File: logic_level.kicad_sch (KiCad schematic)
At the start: 0 parts

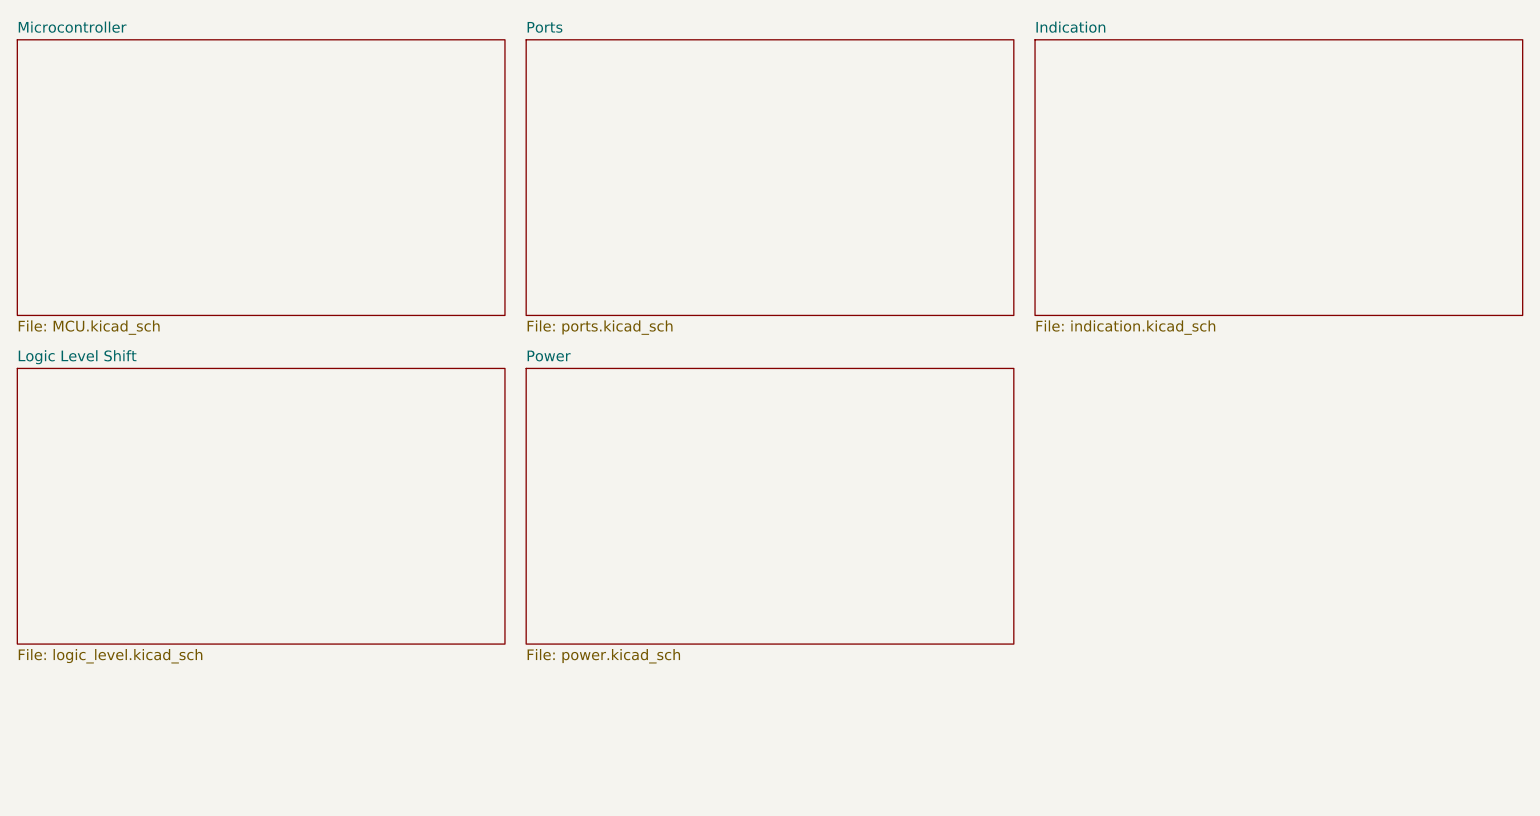
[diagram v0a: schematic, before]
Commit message: Break up schematic into hierarchical sheets
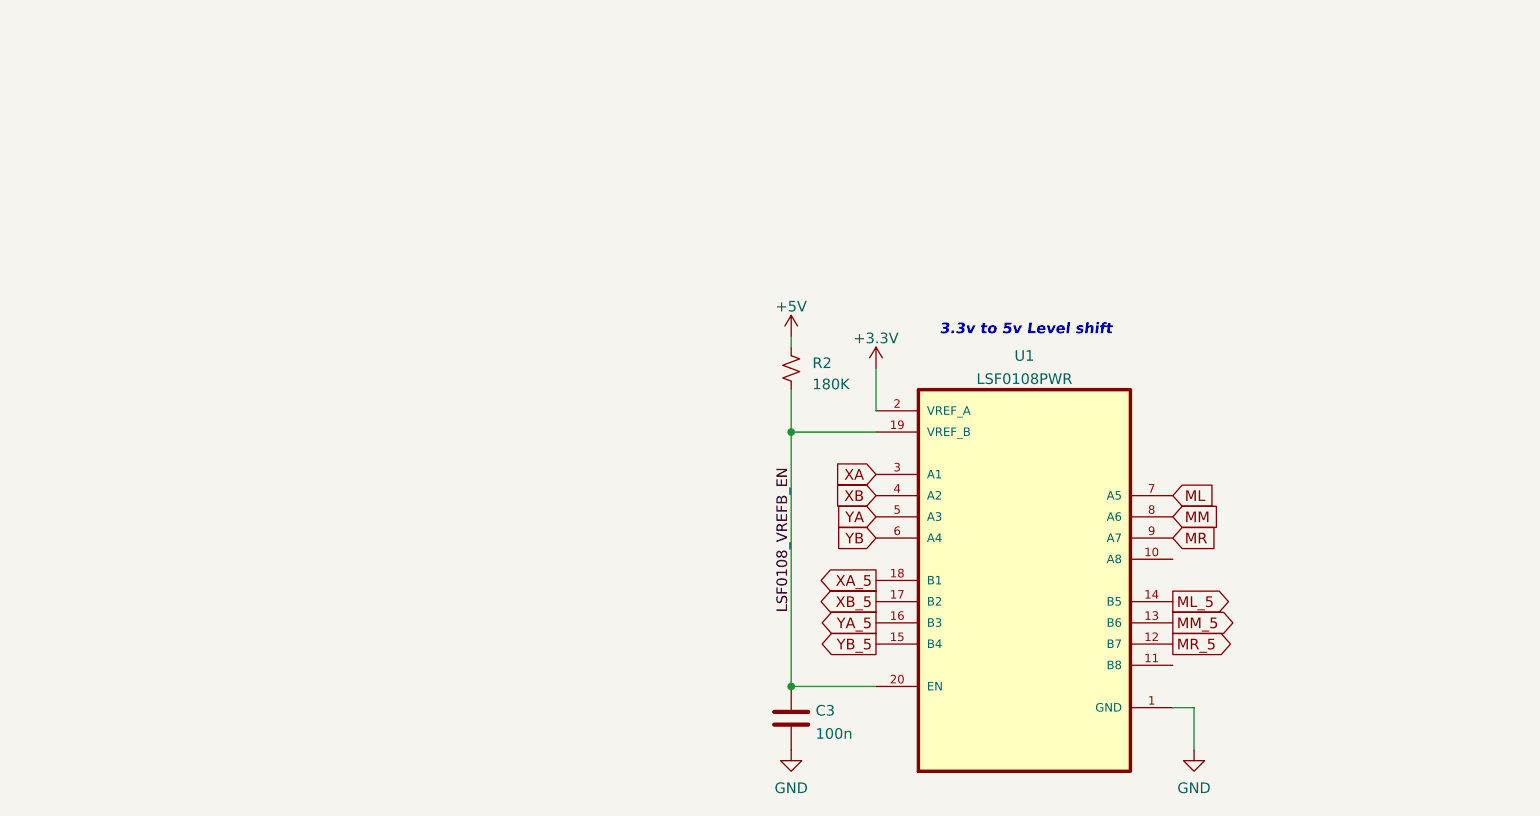
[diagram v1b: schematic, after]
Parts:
- added C3: 100n, Capacitor_SMD:C_0402_1005Metric, symbol Device:C
- added R2: 180K, Resistor_SMD:R_0402_1005Metric, symbol Device:R_Small_US
- added U1: LSF0108PWR, Package_SO:TSSOP-20_4.4x6.5mm_P0.65mm, symbol LSF0108:LSF0108PWR
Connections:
- new net +3V3: U1.2 (VREF_A)
- new net +5V: R2.1
- new net GND: C3.2, U1.1 (GND)
- new net LSF0108_VREFB_EN: C3.1, R2.2, U1.19 (VREF_B), U1.20 (EN)
- new net ML: U1.7 (A5)
- new net ML_5: U1.14 (B5)
- new net MM: U1.8 (A6)
- new net MM_5: U1.13 (B6)
- new net MR: U1.9 (A7)
- new net MR_5: U1.12 (B7)
- new net XA: U1.3 (A1)
- new net XA_5: U1.18 (B1)
- new net XB: U1.4 (A2)
- new net XB_5: U1.17 (B2)
- new net YA: U1.5 (A3)
- new net YA_5: U1.16 (B3)
- new net YB: U1.6 (A4)
- new net YB_5: U1.15 (B4)
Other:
- removed sheet Indication
- removed sheet Logic Level Shift
- removed sheet Microcontroller
- removed sheet Ports
- removed sheet Power
- note added: "3.3v to 5v Level shift"
